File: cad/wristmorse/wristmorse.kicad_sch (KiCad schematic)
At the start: 7 parts, among them J2 Conn_01x03_Pin, J3 Conn_01x03_Pin, J4 AudioJack3_Ground, J5 AudioJack3_Ground, M5stick Conn_01x08, Q1 DTC143E, Q2 DTC143E

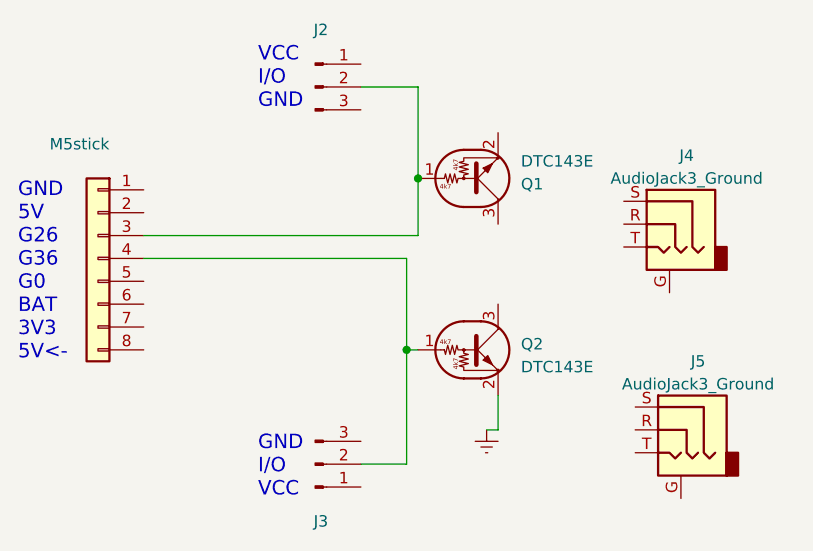
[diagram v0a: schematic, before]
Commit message: added assembly and wiring instructions
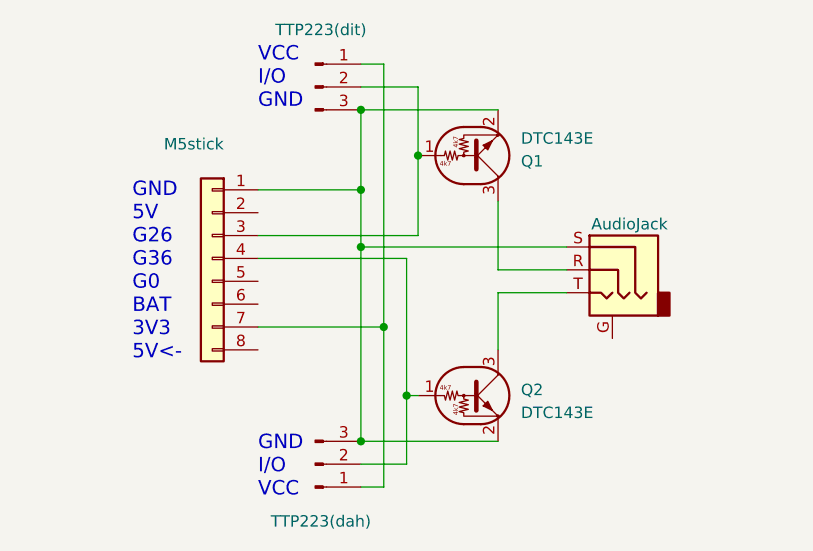
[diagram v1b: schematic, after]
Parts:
- removed J5: AudioJack3_Ground, symbol Connector_Audio:AudioJack3_Ground
- J4: value AudioJack3_Ground -> AudioJack
- renumbered J3 to TTP223(dah), J2 to TTP223(dit)
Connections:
- net GNDREF is gone; now on an unnamed net: Q2.2 (E)
- net at TTP223(dit).1 (Pin_1): now also M5stick.7 (Pin_7), TTP223(dah).1 (Pin_1)
- net at TTP223(dit).3 (Pin_3): now also J4.S, M5stick.1 (Pin_1), Q1.2 (E), TTP223(dah).3 (Pin_3)
- net at J4.R: now also Q1.3 (C)
- net at J4.T: now also Q2.3 (C)
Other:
- moved on the sheet: M5stick, Q1, Q2
